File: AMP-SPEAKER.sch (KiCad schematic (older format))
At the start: 8 parts, among them IC1 MCP4451-103E_ST, U1 AMPLIFIER-PAM8403, U2 AMPLIFIER-PAM8403

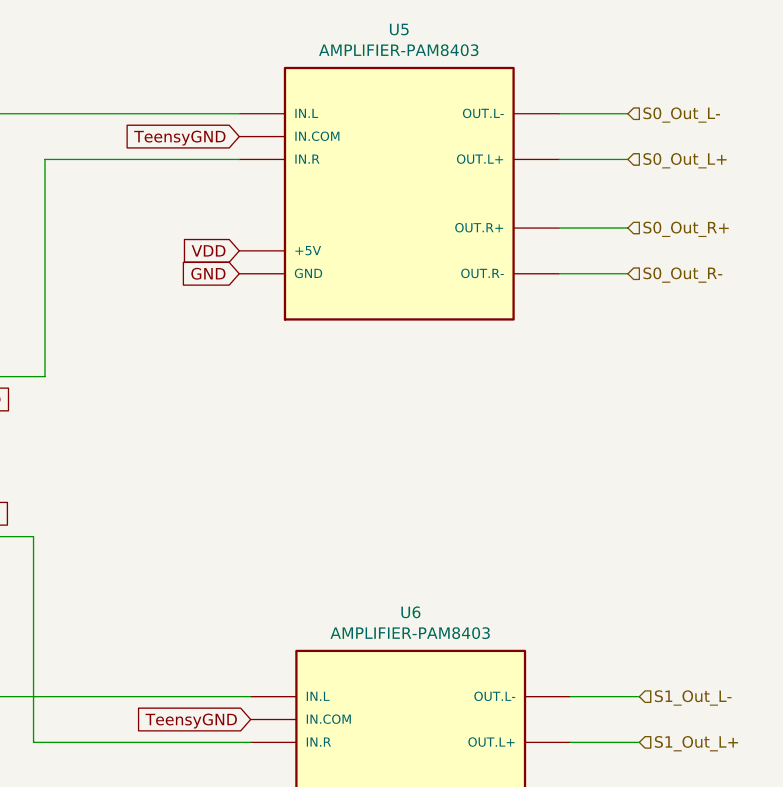
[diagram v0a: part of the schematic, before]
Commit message: Add bottom PCB WIP
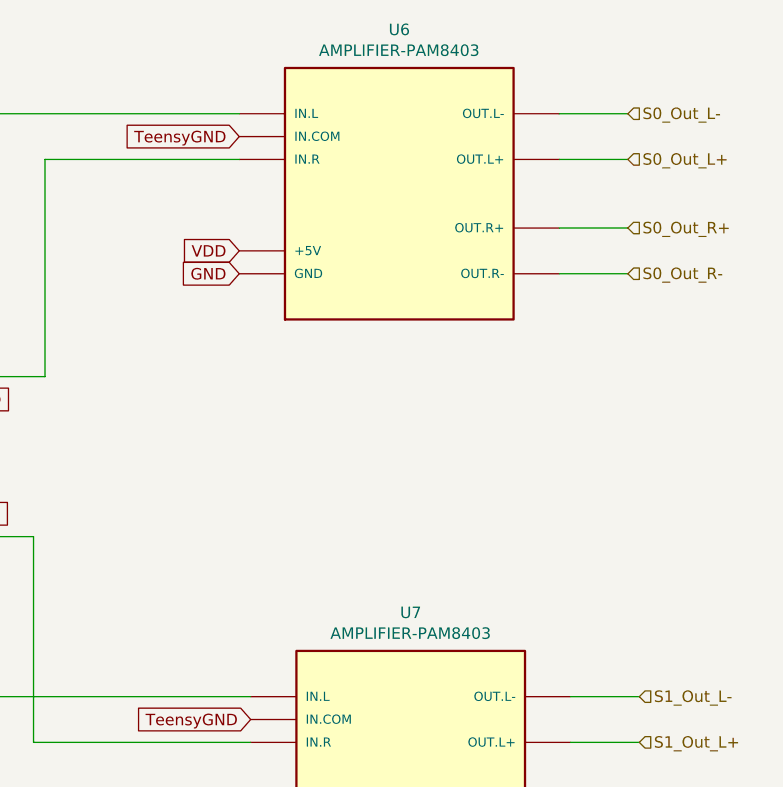
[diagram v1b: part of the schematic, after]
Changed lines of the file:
@@
 $Descr A4 11693 8268
 encoding utf-8
-Sheet 3 4
+Sheet 4 4
 Title "Perception V3.1"
 Date "2021-08-29"
@@
 AR Path="/612B612B/60D0C2F9" Ref="U7"  Part="1"
 AR Path="/60D0C2F9" Ref="U6"  Part="1"
-F 0 "U6" H 7900 5667 50  0000 C CNN
+F 0 "U7" H 7900 5667 50  0000 C CNN
 F 1 "AMPLIFIER-PAM8403" H 7900 5576 50  0000 C CNN
 F 2 "HART:AMPLIFIER-PAM8403" H 7900 5000 50  0001 L BNN
@@
 AR Path="/612B612B/60CD6CAD" Ref="U6"  Part="1"
 AR Path="/60CD6CAD" Ref="U5"  Part="1"
-F 0 "U5" H 7850 3117 50  0000 C CNN
+F 0 "U6" H 7850 3117 50  0000 C CNN
 F 1 "AMPLIFIER-PAM8403" H 7850 3026 50  0000 C CNN
 F 2 "HART:AMPLIFIER-PAM8403" H 7850 2450 50  0001 L BNN

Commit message: Done BOT v3.1
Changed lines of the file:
@@
 $Descr A4 11693 8268
 encoding utf-8
-Sheet 4 4
+Sheet 2 4
 Title "Perception V3.1"
 Date "2021-08-29"
@@
 AR Path="/612B5551/60E20D7F" Ref="R7"  Part="1"
 AR Path="/612B612B/60E20D7F" Ref="R11"  Part="1"
-F 0 "R11" V 2693 3200 50  0001 C CNN
+F 0 "R3" V 2693 3200 50  0001 C CNN
 F 1 "51000" V 2784 3200 50  0001 C CNN
 F 2 "SMD Resistor:R_1206_3216Metric_Pad1.30x1.75mm_HandSolder" V 2830 3200 50  0001 C CNN
@@
 AR Path="/612B5551/60E20D85" Ref="R8"  Part="1"
 AR Path="/612B612B/60E20D85" Ref="R12"  Part="1"
-F 0 "R12" V 2693 4100 50  0001 C CNN
+F 0 "R4" V 2693 4100 50  0001 C CNN
 F 1 "51000" V 2784 4100 50  0001 C CNN
 F 2 "SMD Resistor:R_1206_3216Metric_Pad1.30x1.75mm_HandSolder" V 2830 4100 50  0001 C CNN
@@
 AR Path="/612B5551/60E20D8B" Ref="R10"  Part="1"
 AR Path="/612B612B/60E20D8B" Ref="R14"  Part="1"
-F 0 "R14" V 4293 4100 50  0001 C CNN
+F 0 "R6" V 4293 4100 50  0001 C CNN
 F 1 "51000" V 4384 4100 50  0001 C CNN
 F 2 "SMD Resistor:R_1206_3216Metric_Pad1.30x1.75mm_HandSolder" V 4430 4100 50  0001 C CNN
@@
 AR Path="/612B5551/60E20D91" Ref="R9"  Part="1"
 AR Path="/612B612B/60E20D91" Ref="R13"  Part="1"
-F 0 "R13" V 4293 3200 50  0001 C CNN
+F 0 "R5" V 4293 3200 50  0001 C CNN
 F 1 "51000" V 4384 3200 50  0001 C CNN
 F 2 "SMD Resistor:R_1206_3216Metric_Pad1.30x1.75mm_HandSolder" V 4430 3200 50  0001 C CNN
@@
 AR Path="/612B612B/60D0C2F9" Ref="U7"  Part="1"
 AR Path="/60D0C2F9" Ref="U6"  Part="1"
-F 0 "U7" H 7900 5667 50  0000 C CNN
+F 0 "U3" H 7900 5667 50  0000 C CNN
 F 1 "AMPLIFIER-PAM8403" H 7900 5576 50  0000 C CNN
 F 2 "HART:AMPLIFIER-PAM8403" H 7900 5000 50  0001 L BNN
@@
 AR Path="/612B612B/60CD6CAD" Ref="U6"  Part="1"
 AR Path="/60CD6CAD" Ref="U5"  Part="1"
-F 0 "U6" H 7850 3117 50  0000 C CNN
+F 0 "U2" H 7850 3117 50  0000 C CNN
 F 1 "AMPLIFIER-PAM8403" H 7850 3026 50  0000 C CNN
 F 2 "HART:AMPLIFIER-PAM8403" H 7850 2450 50  0001 L BNN
@@
 AR Path="/612B5551/60E20D4C" Ref="IC2"  Part="1"
 AR Path="/612B612B/60E20D4C" Ref="IC3"  Part="1"
-F 0 "IC3" H 3700 3465 50  0001 C CNN
+F 0 "IC1" H 3700 3465 50  0001 C CNN
 F 1 "MCP4451-103E_ST" H 3700 3374 50  0000 C CNN
 F 2 "MCP4451:SOP65P640X120-20N" H 4200 3300 50  0001 L CNN
@@
 AR Path="/60B2095D/61363135" Ref="C1"  Part="1"
 AR Path="/612FF705/61363135" Ref="C3"  Part="1"
-F 0 "C3" H 5472 3604 50  0000 R CNN
+F 0 "C1" H 5472 3604 50  0000 R CNN
 F 1 "100nF" H 5472 3695 50  0000 R CNN
 F 2 "SMD Capacitor:C_1206_3216Metric_Pad1.33x1.80mm_HandSolder" H 5650 3650 50  0001 C CNN

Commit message: Cleanup symbols and libraries and add separate submodule for kicad-libaries
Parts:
- R3, R4, R5, R6: symbol v3-rescue:R-Device -> pspice:R
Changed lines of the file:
@@
 $Descr A4 11693 8268
 encoding utf-8
-Sheet 2 4
+Sheet 4 4
 Title "Perception V3.1"
 Date "2021-08-29"
@@
 	2750 3500 3050 3500
 $Comp
-L v3-rescue:R-Device R?
+L pspice:R R?
 U 1 1 60E20D7F
-P 2900 3200
+P 2800 3200
 AR Path="/60E20D7F" Ref="R?"  Part="1"
 AR Path="/60B3C664/60E20D7F" Ref="R?"  Part="1"
@@
 AR Path="/612B5551/60E20D7F" Ref="R7"  Part="1"
 AR Path="/612B612B/60E20D7F" Ref="R11"  Part="1"
-F 0 "R3" V 2693 3200 50  0001 C CNN
-F 1 "51000" V 2784 3200 50  0001 C CNN
-F 2 "SMD Resistor:R_1206_3216Metric_Pad1.30x1.75mm_HandSolder" V 2830 3200 50  0001 C CNN
-F 3 "~" H 2900 3200 50  0001 C CNN
-	1    2900 3200
+F 0 "R11" V 2593 3200 50  0001 C CNN
+F 1 "51000" V 2684 3200 50  0001 C CNN
+F 2 "SMD Resistor:R_1206_3216Metric_Pad1.30x1.75mm_HandSolder" V 2730 3200 50  0001 C CNN
+F 3 "~" H 2800 3200 50  0001 C CNN
+	1    2800 3200
 	0    1    1    0
 $EndComp
 $Comp
-L v3-rescue:R-Device R?
+L pspice:R R?
 U 1 1 60E20D85
-P 2900 4100
+P 2800 4100
 AR Path="/60E20D85" Ref="R?"  Part="1"
 AR Path="/60B3C664/60E20D85" Ref="R?"  Part="1"
@@
 AR Path="/612B5551/60E20D85" Ref="R8"  Part="1"
 AR Path="/612B612B/60E20D85" Ref="R12"  Part="1"
-F 0 "R4" V 2693 4100 50  0001 C CNN
-F 1 "51000" V 2784 4100 50  0001 C CNN
-F 2 "SMD Resistor:R_1206_3216Metric_Pad1.30x1.75mm_HandSolder" V 2830 4100 50  0001 C CNN
-F 3 "~" H 2900 4100 50  0001 C CNN
-	1    2900 4100
+F 0 "R12" V 2593 4100 50  0001 C CNN
+F 1 "51000" V 2684 4100 50  0001 C CNN
+F 2 "SMD Resistor:R_1206_3216Metric_Pad1.30x1.75mm_HandSolder" V 2730 4100 50  0001 C CNN
+F 3 "~" H 2800 4100 50  0001 C CNN
+	1    2800 4100
 	0    1    1    0
 $EndComp
 $Comp
-L v3-rescue:R-Device R?
+L pspice:R R?
 U 1 1 60E20D8B
-P 4500 4100
+P 4600 4100
 AR Path="/60E20D8B" Ref="R?"  Part="1"
 AR Path="/60B3C664/60E20D8B" Ref="R?"  Part="1"
@@
 AR Path="/612B5551/60E20D8B" Ref="R10"  Part="1"
 AR Path="/612B612B/60E20D8B" Ref="R14"  Part="1"
-F 0 "R6" V 4293 4100 50  0001 C CNN
-F 1 "51000" V 4384 4100 50  0001 C CNN
-F 2 "SMD Resistor:R_1206_3216Metric_Pad1.30x1.75mm_HandSolder" V 4430 4100 50  0001 C CNN
-F 3 "~" H 4500 4100 50  0001 C CNN
-	1    4500 4100
+F 0 "R14" V 4393 4100 50  0001 C CNN
+F 1 "51000" V 4484 4100 50  0001 C CNN
+F 2 "SMD Resistor:R_1206_3216Metric_Pad1.30x1.75mm_HandSolder" V 4530 4100 50  0001 C CNN
+F 3 "~" H 4600 4100 50  0001 C CNN
+	1    4600 4100
 	0    1    1    0
 $EndComp
 $Comp
-L v3-rescue:R-Device R?
+L pspice:R R?
 U 1 1 60E20D91
-P 4500 3200
+P 4600 3200
 AR Path="/60E20D91" Ref="R?"  Part="1"
 AR Path="/60B3C664/60E20D91" Ref="R?"  Part="1"
@@
 AR Path="/612B5551/60E20D91" Ref="R9"  Part="1"
 AR Path="/612B612B/60E20D91" Ref="R13"  Part="1"
-F 0 "R5" V 4293 3200 50  0001 C CNN
-F 1 "51000" V 4384 3200 50  0001 C CNN
-F 2 "SMD Resistor:R_1206_3216Metric_Pad1.30x1.75mm_HandSolder" V 4430 3200 50  0001 C CNN
-F 3 "~" H 4500 3200 50  0001 C CNN
-	1    4500 3200
+F 0 "R13" V 4393 3200 50  0001 C CNN
+F 1 "51000" V 4484 3200 50  0001 C CNN
+F 2 "SMD Resistor:R_1206_3216Metric_Pad1.30x1.75mm_HandSolder" V 4530 3200 50  0001 C CNN
+F 3 "~" H 4600 3200 50  0001 C CNN
+	1    4600 3200
 	0    1    1    0
 $EndComp
@@
 Text HLabel 3050 3700 0    50   Input ~ 0
 SDA
-Text HLabel 2750 4100 0    50   Input ~ 0
+Text HLabel 2550 4100 0    50   Input ~ 0
 P1A
-Text HLabel 4650 4100 2    50   Input ~ 0
+Text HLabel 4850 4100 2    50   Input ~ 0
 P0A
-Text HLabel 4650 3200 2    50   Input ~ 0
+Text HLabel 4850 3200 2    50   Input ~ 0
 P2A
-Text HLabel 2750 3200 0    50   Input ~ 0
+Text HLabel 2550 3200 0    50   Input ~ 0
 P3A
 NoConn ~ 4350 3700
@@
 AR Path="/612B612B/60D0C2F9" Ref="U7"  Part="1"
 AR Path="/60D0C2F9" Ref="U6"  Part="1"
-F 0 "U3" H 7900 5667 50  0000 C CNN
+F 0 "U7" H 7900 5667 50  0000 C CNN
 F 1 "AMPLIFIER-PAM8403" H 7900 5576 50  0000 C CNN
 F 2 "HART:AMPLIFIER-PAM8403" H 7900 5000 50  0001 L BNN
@@
 AR Path="/612B612B/60CD6CAD" Ref="U6"  Part="1"
 AR Path="/60CD6CAD" Ref="U5"  Part="1"
-F 0 "U2" H 7850 3117 50  0000 C CNN
+F 0 "U6" H 7850 3117 50  0000 C CNN
 F 1 "AMPLIFIER-PAM8403" H 7850 3026 50  0000 C CNN
 F 2 "HART:AMPLIFIER-PAM8403" H 7850 2450 50  0001 L BNN
@@
 AR Path="/612B5551/60E20D4C" Ref="IC2"  Part="1"
 AR Path="/612B612B/60E20D4C" Ref="IC3"  Part="1"
-F 0 "IC1" H 3700 3465 50  0001 C CNN
+F 0 "IC3" H 3700 3465 50  0001 C CNN
 F 1 "MCP4451-103E_ST" H 3700 3374 50  0000 C CNN
 F 2 "MCP4451:SOP65P640X120-20N" H 4200 3300 50  0001 L CNN
@@
 AR Path="/60B2095D/61363135" Ref="C1"  Part="1"
 AR Path="/612FF705/61363135" Ref="C3"  Part="1"
-F 0 "C1" H 5472 3604 50  0000 R CNN
+AR Path="/61363135" Ref="C1"  Part="1"
+F 0 "C3" H 5472 3604 50  0000 R CNN
 F 1 "100nF" H 5472 3695 50  0000 R CNN
 F 2 "SMD Capacitor:C_1206_3216Metric_Pad1.33x1.80mm_HandSolder" H 5650 3650 50  0001 C CNN

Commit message: V3.2 start
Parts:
- removed U1, U2: AMPLIFIER-PAM8403, HART:AMPLIFIER-PAM8403, symbol PAM8403-1:AMPLIFIER-PAM8403
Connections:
- net sheet61A7FB4F/IN.L: now reaches IC1.2 (P3W)
- net sheet61A7FB4F/IN.R: now reaches IC1.19 (P2W)
- net PAM8406/IN.L: now reaches IC1.9 (P1W)
- net PAM8406/IN.R: now reaches IC1.12 (P0W)
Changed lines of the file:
@@
 $Descr A4 11693 8268
 encoding utf-8
-Sheet 4 4
+Sheet 17 19
 Title "Perception V3.1"
 Date "2021-08-29"
@@
 AR Path="/612B5551/60E20D7F" Ref="R7"  Part="1"
 AR Path="/612B612B/60E20D7F" Ref="R11"  Part="1"
-F 0 "R11" V 2593 3200 50  0001 C CNN
+AR Path="/61A95E2F/60E20D7F" Ref="R17"  Part="1"
+AR Path="/61A95E42/60E20D7F" Ref="R21"  Part="1"
+AR Path="/61A95E54/60E20D7F" Ref="R25"  Part="1"
+F 0 "R25" V 2593 3200 50  0001 C CNN
 F 1 "51000" V 2684 3200 50  0001 C CNN
 F 2 "SMD Resistor:R_1206_3216Metric_Pad1.30x1.75mm_HandSolder" V 2730 3200 50  0001 C CNN
@@
 AR Path="/612B5551/60E20D85" Ref="R8"  Part="1"
 AR Path="/612B612B/60E20D85" Ref="R12"  Part="1"
-F 0 "R12" V 2593 4100 50  0001 C CNN
+AR Path="/61A95E2F/60E20D85" Ref="R18"  Part="1"
+AR Path="/61A95E42/60E20D85" Ref="R22"  Part="1"
+AR Path="/61A95E54/60E20D85" Ref="R26"  Part="1"
+F 0 "R26" V 2593 4100 50  0001 C CNN
 F 1 "51000" V 2684 4100 50  0001 C CNN
 F 2 "SMD Resistor:R_1206_3216Metric_Pad1.30x1.75mm_HandSolder" V 2730 4100 50  0001 C CNN
@@
 AR Path="/612B5551/60E20D8B" Ref="R10"  Part="1"
 AR Path="/612B612B/60E20D8B" Ref="R14"  Part="1"
-F 0 "R14" V 4393 4100 50  0001 C CNN
+AR Path="/61A95E2F/60E20D8B" Ref="R20"  Part="1"
+AR Path="/61A95E42/60E20D8B" Ref="R24"  Part="1"
+AR Path="/61A95E54/60E20D8B" Ref="R28"  Part="1"
+F 0 "R28" V 4393 4100 50  0001 C CNN
 F 1 "51000" V 4484 4100 50  0001 C CNN
 F 2 "SMD Resistor:R_1206_3216Metric_Pad1.30x1.75mm_HandSolder" V 4530 4100 50  0001 C CNN
@@
 AR Path="/612B5551/60E20D91" Ref="R9"  Part="1"
 AR Path="/612B612B/60E20D91" Ref="R13"  Part="1"
-F 0 "R13" V 4393 3200 50  0001 C CNN
+AR Path="/61A95E2F/60E20D91" Ref="R19"  Part="1"
+AR Path="/61A95E42/60E20D91" Ref="R23"  Part="1"
+AR Path="/61A95E54/60E20D91" Ref="R27"  Part="1"
+F 0 "R27" V 4393 3200 50  0001 C CNN
 F 1 "51000" V 4484 3200 50  0001 C CNN
 F 2 "SMD Resistor:R_1206_3216Metric_Pad1.30x1.75mm_HandSolder" V 4530 3200 50  0001 C CNN
@@
 Text HLabel 2750 3500 0    50   Input ~ 0
 A0
-$Comp
-L PAM8403-1:AMPLIFIER-PAM8403 U?
-U 1 1 60D0C2F9
-P 7900 5000
-AR Path="/60B20945/60D0C2F9" Ref="U?"  Part="1"
-AR Path="/60B2094D/60D0C2F9" Ref="U?"  Part="1"
-AR Path="/60B20955/60D0C2F9" Ref="U?"  Part="1"
-AR Path="/60B2095D/60D0C2F9" Ref="U2"  Part="1"
-AR Path="/60B20965/60D0C2F9" Ref="U?"  Part="1"
-AR Path="/60B2096D/60D0C2F9" Ref="U?"  Part="1"
-AR Path="/612FD936/60D0C2F9" Ref="U4"  Part="1"
-AR Path="/612FF705/60D0C2F9" Ref="U6"  Part="1"
-AR Path="/612C106E/60D0C2F9" Ref="U3"  Part="1"
-AR Path="/612B5551/60D0C2F9" Ref="U5"  Part="1"
-AR Path="/612B612B/60D0C2F9" Ref="U7"  Part="1"
-AR Path="/60D0C2F9" Ref="U6"  Part="1"
-F 0 "U7" H 7900 5667 50  0000 C CNN
-F 1 "AMPLIFIER-PAM8403" H 7900 5576 50  0000 C CNN
-F 2 "HART:AMPLIFIER-PAM8403" H 7900 5000 50  0001 L BNN
-F 3 "" H 7900 5000 50  0001 L BNN
-	1    7900 5000
-	1    0    0    -1
-$EndComp
-Text GLabel 7200 5300 0    50   Input ~ 0
-VDD
-Text GLabel 7200 5400 0    50   Input ~ 0
-GND
-Wire Wire Line
-	4350 4000 6250 4000
-Wire Wire Line
-	6250 4000 6250 4900
-Wire Wire Line
-	6250 4900 7200 4900
-Wire Wire Line
-	7200 4700 2150 4700
-Wire Wire Line
-	2150 4000 2150 4700
-Text GLabel 7200 4800 0    50   Input ~ 0
-TeensyGND
 NoConn ~ 4350 3800
 Text HLabel 3050 3600 0    50   Input ~ 0
 SCL
-Text HLabel 8900 4700 2    50   Input ~ 0
-S1_Out_L-
-Text HLabel 8900 4900 2    50   Input ~ 0
-S1_Out_L+
-Text HLabel 8900 5200 2    50   Input ~ 0
-S1_Out_R+
-Text HLabel 8900 5400 2    50   Input ~ 0
-S1_Out_R-
-Wire Wire Line
-	8600 5400 8900 5400
-Wire Wire Line
-	8600 5200 8900 5200
-Wire Wire Line
-	8600 4900 8900 4900
-Wire Wire Line
-	8600 4700 8900 4700
-Wire Wire Line
-	6300 2350 6300 3300
-Wire Wire Line
-	5850 2150 5850 3000
-Wire Wire Line
-	8550 2150 8850 2150
-Wire Wire Line
-	8550 2350 8850 2350
-Wire Wire Line
-	8550 2650 8850 2650
-Wire Wire Line
-	8550 2850 8850 2850
-Text HLabel 8850 2850 2    50   Input ~ 0
-S0_Out_R-
-Text HLabel 8850 2650 2    50   Input ~ 0
-S0_Out_R+
-Text HLabel 8850 2350 2    50   Input ~ 0
-S0_Out_L+
-Text HLabel 8850 2150 2    50   Input ~ 0
-S0_Out_L-
-Text GLabel 7150 2850 0    50   Input ~ 0
-GND
-Text GLabel 7150 2750 0    50   Input ~ 0
-VDD
-Wire Wire Line
-	6300 2350 7150 2350
-Wire Wire Line
-	7150 2150 5850 2150
-$Comp
-L PAM8403-1:AMPLIFIER-PAM8403 U?
-U 1 1 60CD6CAD
-P 7850 2450
-AR Path="/60B20945/60CD6CAD" Ref="U?"  Part="1"
-AR Path="/60B2094D/60CD6CAD" Ref="U?"  Part="1"
-AR Path="/60B20955/60CD6CAD" Ref="U?"  Part="1"
-AR Path="/60B2095D/60CD6CAD" Ref="U1"  Part="1"
-AR Path="/60B20965/60CD6CAD" Ref="U?"  Part="1"
-AR Path="/60B2096D/60CD6CAD" Ref="U?"  Part="1"
-AR Path="/612FD936/60CD6CAD" Ref="U3"  Part="1"
-AR Path="/612FF705/60CD6CAD" Ref="U5"  Part="1"
-AR Path="/612C106E/60CD6CAD" Ref="U2"  Part="1"
-AR Path="/612B5551/60CD6CAD" Ref="U4"  Part="1"
-AR Path="/612B612B/60CD6CAD" Ref="U6"  Part="1"
-AR Path="/60CD6CAD" Ref="U5"  Part="1"
-F 0 "U6" H 7850 3117 50  0000 C CNN
-F 1 "AMPLIFIER-PAM8403" H 7850 3026 50  0000 C CNN
-F 2 "HART:AMPLIFIER-PAM8403" H 7850 2450 50  0001 L BNN
-F 3 "" H 7850 2450 50  0001 L BNN
-	1    7850 2450
-	1    0    0    -1
-$EndComp
-Text GLabel 7150 2250 0    50   Input ~ 0
-TeensyGND
 Text HLabel 4650 3600 2    50   Input ~ 0
 A1
@@
 AR Path="/612B5551/60E20D4C" Ref="IC2"  Part="1"
 AR Path="/612B612B/60E20D4C" Ref="IC3"  Part="1"
-F 0 "IC3" H 3700 3465 50  0001 C CNN
+AR Path="/61A95E2F/60E20D4C" Ref="IC10"  Part="1"
+AR Path="/61A95E42/60E20D4C" Ref="IC13"  Part="1"
+AR Path="/61A95E54/60E20D4C" Ref="IC16"  Part="1"
+F 0 "IC16" H 3700 3465 50  0001 C CNN
 F 1 "MCP4451-103E_ST" H 3700 3374 50  0000 C CNN
 F 2 "MCP4451:SOP65P640X120-20N" H 4200 3300 50  0001 L CNN
@@
 AR Path="/612FF705/61363135" Ref="C3"  Part="1"
 AR Path="/61363135" Ref="C1"  Part="1"
-F 0 "C3" H 5472 3604 50  0000 R CNN
+AR Path="/61A95E2F/61363135" Ref="C28"  Part="1"
+AR Path="/61A95E42/61363135" Ref="C37"  Part="1"
+AR Path="/61A95E54/61363135" Ref="C46"  Part="1"
+F 0 "C46" H 5472 3604 50  0000 R CNN
 F 1 "100nF" H 5472 3695 50  0000 R CNN
 F 2 "SMD Capacitor:C_1206_3216Metric_Pad1.33x1.80mm_HandSolder" H 5650 3650 50  0001 C CNN
@@
 Wire Wire Line
 	4350 3400 5650 3400
+Text GLabel 7250 2250 0    50   Input ~ 0
+TeensyGND
+Text HLabel 8600 2400 2    50   Output ~ 0
+S0_Out_R-
+Text HLabel 8600 2550 2    50   Output ~ 0
+S0_Out_R+
+Text HLabel 8600 2250 2    50   Output ~ 0
+S0_Out_L+
+Text HLabel 8600 2100 2    50   Output ~ 0
+S0_Out_L-
+Wire Wire Line
+	2150 4000 2150 4650
+Text GLabel 7250 4800 0    50   Input ~ 0
+TeensyGND
+Wire Wire Line
+	6300 4950 7250 4950
+Wire Wire Line
+	8300 4950 8600 4950
+Wire Wire Line
+	8300 5100 8600 5100
+Wire Wire Line
+	8300 4800 8600 4800
+Wire Wire Line
+	8300 4650 8600 4650
+Text HLabel 8600 4650 2    50   Output ~ 0
+S1_Out_L-
+Text HLabel 8600 4800 2    50   Output ~ 0
+S1_Out_L+
+Text HLabel 8600 5100 2    50   Output ~ 0
+S1_Out_R+
+Text HLabel 8600 4950 2    50   Output ~ 0
+S1_Out_R-
+$Sheet
+S 7250 4500 1050 750
+U 61A6AB67
+F0 "PAM8406" 50
+F1 "PAM8406.sch" 50
+F2 "OUT_L+" O R 8300 4800 50
+F3 "OUT_L-" O R 8300 4650 50
+F4 "OUT_R+" O R 8300 5100 50
+F5 "OUT_R-" O R 8300 4950 50
+F6 "IN.L" I L 7250 4650 50
+F7 "IN.R" I L 7250 4950 50
+F8 "IN.COM" U L 7250 4800 50
+$EndSheet
+Wire Wire Line
+	4350 4000 6300 4000
+Wire Wire Line
+	6300 4000 6300 4950
+Wire Wire Line
+	2150 4650 7250 4650
+Wire Wire Line
+	8300 2400 8600 2400
+Wire Wire Line
+	8300 2550 8600 2550
+Wire Wire Line
+	8300 2250 8600 2250
+Wire Wire Line
+	8300 2100 8600 2100
+$Sheet
+S 7250 1950 1050 750
+U 61A7FB60
+F0 "sheet61A7FB4F" 50
+F1 "PAM8406.sch" 50
+F2 "OUT_L+" O R 8300 2250 50
+F3 "OUT_L-" O R 8300 2100 50
+F4 "OUT_R+" O R 8300 2550 50
+F5 "OUT_R-" O R 8300 2400 50
+F6 "IN.L" I L 7250 2100 50
+F7 "IN.R" I L 7250 2400 50
+F8 "IN.COM" U L 7250 2250 50
+$EndSheet
+Wire Wire Line
+	6300 2400 6300 3300
+Wire Wire Line
+	5850 2100 5850 3000
+Wire Wire Line
+	6300 2400 7250 2400
+Wire Wire Line
+	5850 2100 7250 2100
 $EndSCHEMATC
